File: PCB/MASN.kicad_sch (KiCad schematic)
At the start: 39 parts, among them J1 73412-0110, J1 USB4500-03-0-A, J3 5044490207, J4 SIM8051-6-0-14-00, J6 5044490507, J7 5044490207, J8 73412-0110, J9 5051100792, SW1 PTS636SM43JSMTR LFS, U1 MAX-M10S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

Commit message: Licenses update
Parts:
- U3: value MCP1700T-2302E/TT -> MCP1700T-2302E/TT
- renumbered J1 to J2, U1 to U4
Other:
- note added: "Copyright (C) 2026 - G. Quintero This program/design is free software: you can redistribute it and/or modify it under the terms of the following licenses: FIRMWARE/SOFTWARE: Licensed under the GNU General Public License as published by the Free Software Foundation, either version 3 of the License, or (at your option) any later version. SPDX-License-Identifier: GPL-3.0-or-later HARDWARE: Licensed 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"
- moved on the sheet: J4, J8

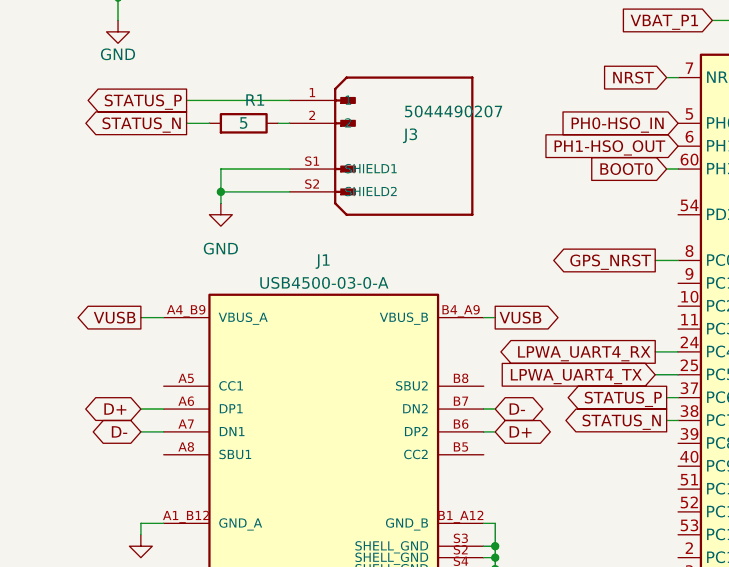
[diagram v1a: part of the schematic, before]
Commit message: Delta-coding, automatic IMEI and timestamp working (1 s samples)
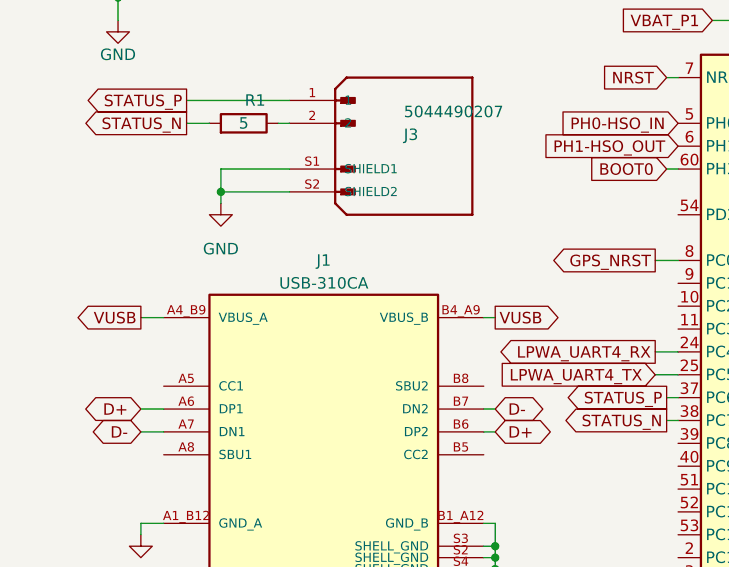
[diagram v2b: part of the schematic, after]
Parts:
- J1: value USB4500-03-0-A -> USB-310CA; footprint GCT_USB4500-03-0-A_REVA -> Customs:USB-C-SMD_20P-P0.50-L6.5-W11.2
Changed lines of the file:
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@@
 			)
 		)
-		(property "Value" "USB4500-03-0-A"
+		(property "Value" "USB-310CA"
 			(at 41.91 123.19 0)
 			(effects
@@
 			)
 		)
-		(property "Footprint" "GCT_USB4500-03-0-A_REVA"
+		(property "Footprint" "Customs:USB-C-SMD_20P-P0.50-L6.5-W11.2"
 			(at 41.91 139.7 0)
 			(effects
